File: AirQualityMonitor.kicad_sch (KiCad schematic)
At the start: 34 parts, among them J1 USB_C_Receptacle_USB2.0_16P, U1 TLV70033DDCR, U2 TLV70036DDCR, U3 USBLC6-2SC6, U4 TPS2553DDBVR

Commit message: Use a different LED with better forward voltage
Change the main MCU LED to a one with better forward voltage.
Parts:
- D1: Height 2.44 -> (none)
- U1, U2: Height 1.1 -> (none)
- U4: Height 1.45 -> (none)

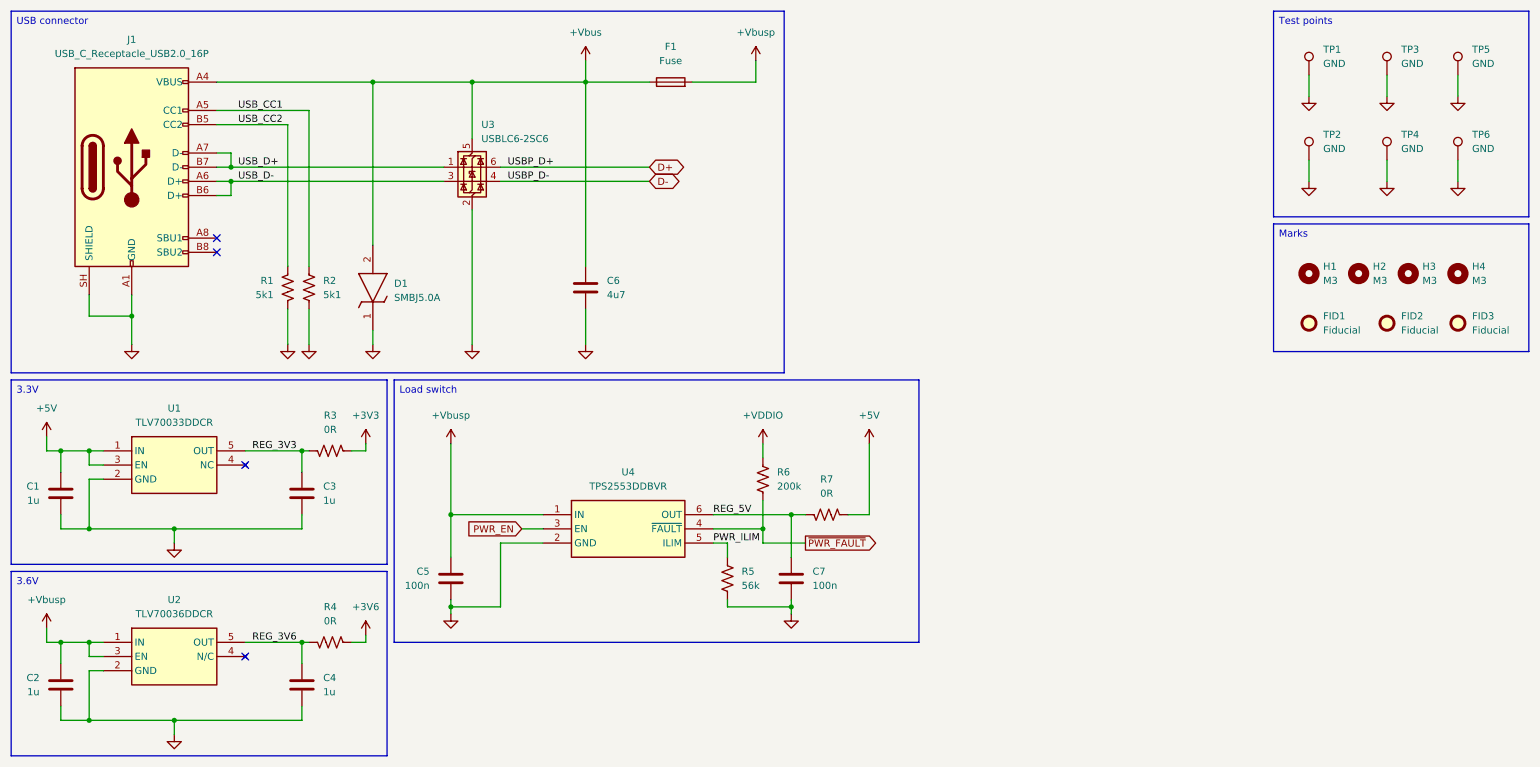
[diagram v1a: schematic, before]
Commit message: Move sheets to a separate folder
The board sheet files have been moved to a sheet folder to make
the repository more readable.
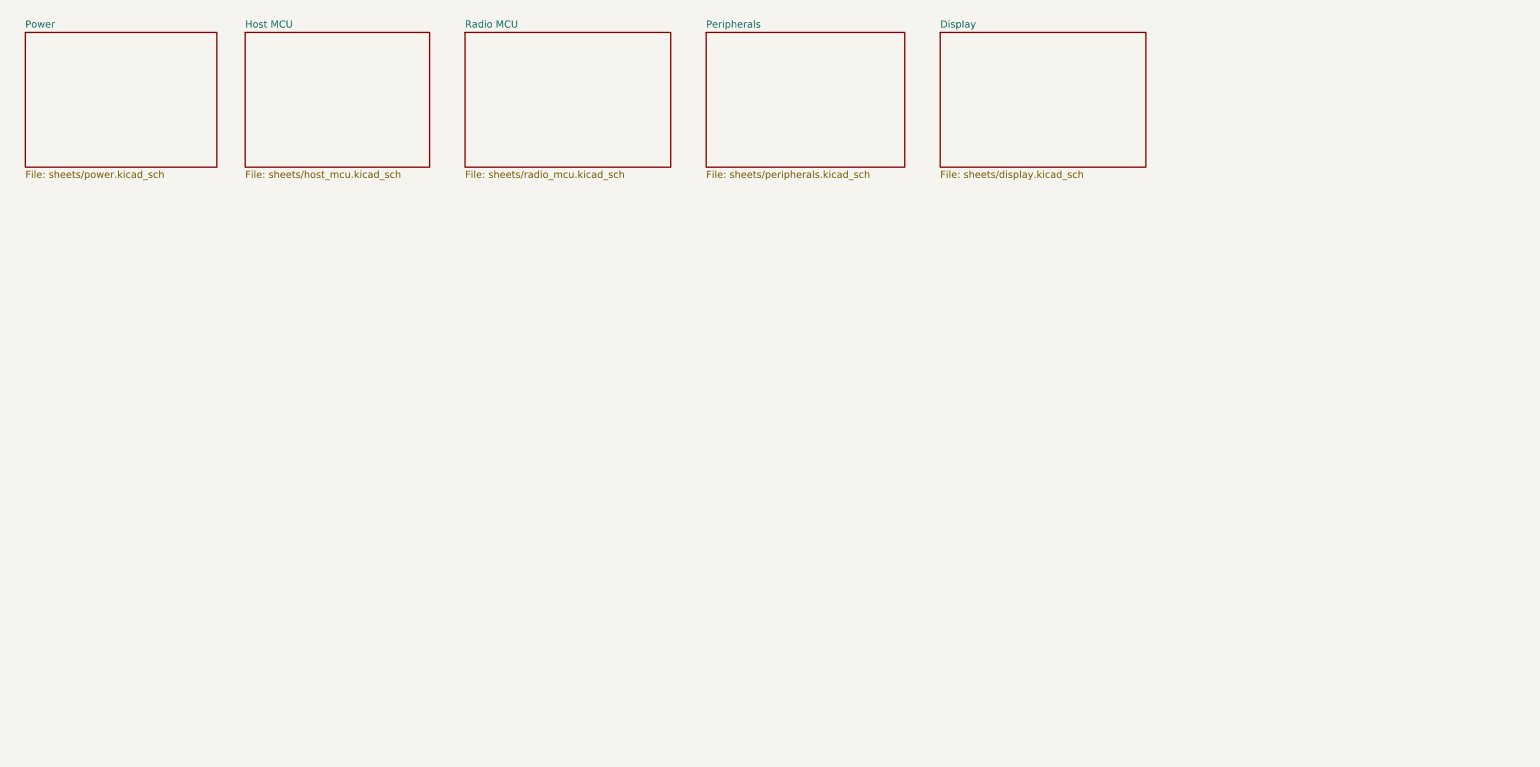
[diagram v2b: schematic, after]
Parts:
- removed C1, C2, C3, C4: 1u, Capacitor_SMD:C_0402_1005Metric, symbol Device:C
- removed C5, C7: 100n, Capacitor_SMD:C_0603_1608Metric, symbol Device:C
- removed C6: 4u7, Capacitor_SMD:C_0603_1608Metric, symbol Device:C
- removed D1: SMBJ5.0A, SMBJ5.0A:DIOM5436X244N, symbol SMBJ5_0A:SMBJ5.0A
- removed F1: Fuse, MyLib:Fuse_SF-1206F, symbol Device:Fuse
- removed FID1, FID2, FID3: Fiducial, Fiducial:Fiducial_1mm_Mask2mm, symbol Mechanical:Fiducial
- removed H1, H2, H3, H4: M3, MountingHole:MountingHole_3mm, symbol Mechanical:MountingHole
- removed J1: USB_C_Receptacle_USB2.0_16P, MyLib:USB_C_Receptacle_UJ20-C-H-G-SMT-P16-TR, symbol Connector:USB_C_Receptacle_USB2.0_16P
- removed R1, R2: 5k1, Resistor_SMD:R_0603_1608Metric, symbol Device:R_US
- removed R3, R4, R7: 0R, Resistor_SMD:R_0603_1608Metric, symbol Device:R_US
- removed R5: 56k, Resistor_SMD:R_0402_1005Metric, symbol Device:R_US
- removed R6: 200k, Resistor_SMD:R_0805_2012Metric, symbol Device:R_US
- removed TP1, TP2, TP3, TP4, TP5, TP6: GND, TestPoint:TestPoint_Pad_D1.0mm, symbol Connector:TestPoint
- removed U1: TLV70033DDCR, TLV70033DDCR:SOT95P280X110-5N, symbol TLV70033DDCR:TLV70033DDCR
- removed U2: TLV70036DDCR, TLV70036DDCR:SOT95P280X110-5N, symbol TLV70036DDCR:TLV70036DDCR
- removed U3: USBLC6-2SC6, Package_TO_SOT_SMD:SOT-23-6, symbol Power_Protection:USBLC6-2SC6
- removed U4: TPS2553DDBVR, TPS2553DDBVR:SOT95P280X145-6N, symbol TPS2553DDBVR:TPS2553DDBVR
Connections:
- no-connect marks 4 -> 0
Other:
- added sheet Display (sheets/display.kicad_sch)
- added sheet Host MCU (sheets/host_mcu.kicad_sch)
- added sheet Peripherals (sheets/peripherals.kicad_sch)
- added sheet Power (sheets/power.kicad_sch)
- added sheet Radio MCU (sheets/radio_mcu.kicad_sch)
